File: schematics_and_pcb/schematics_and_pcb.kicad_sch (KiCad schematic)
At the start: 84 parts, among them J1 RND 205-00623, J2 RND 205-00627, SW1 RND 210-00210, U1 MIC5235YM5-TR, U2 AP2125N-3.3TRG1, U3 PWM3389DM-T3QU, U4 STM32F411RETx, Y1 YLFXTAL029370

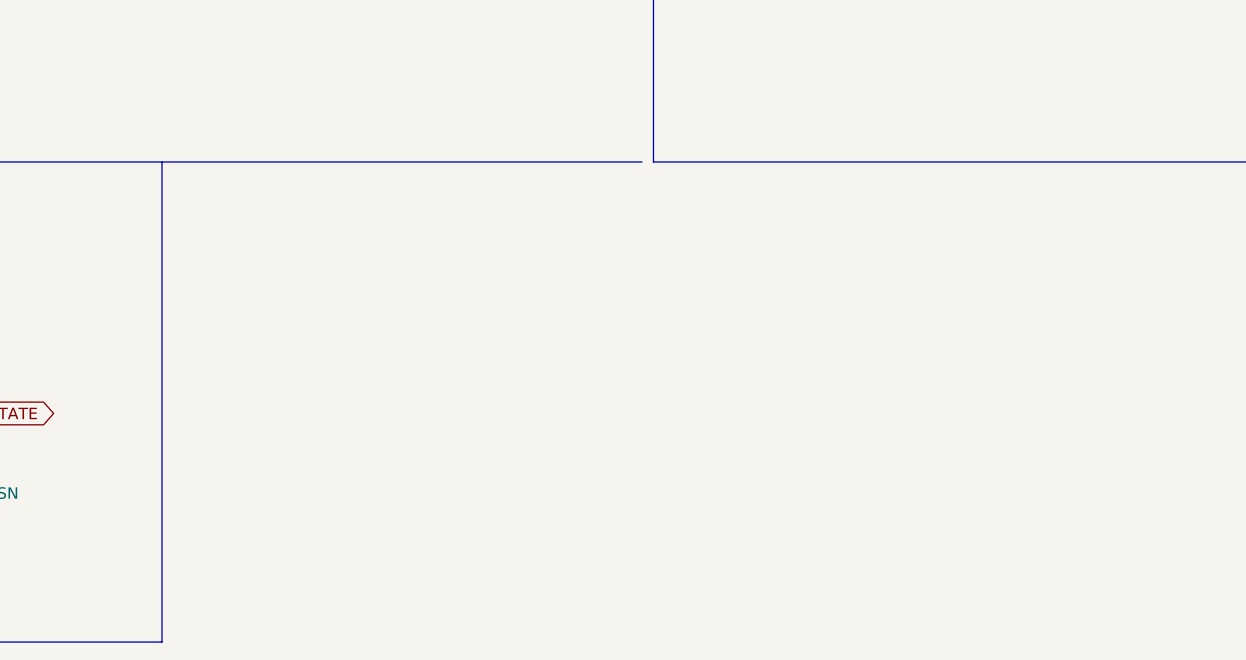
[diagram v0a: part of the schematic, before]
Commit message: added motor driver
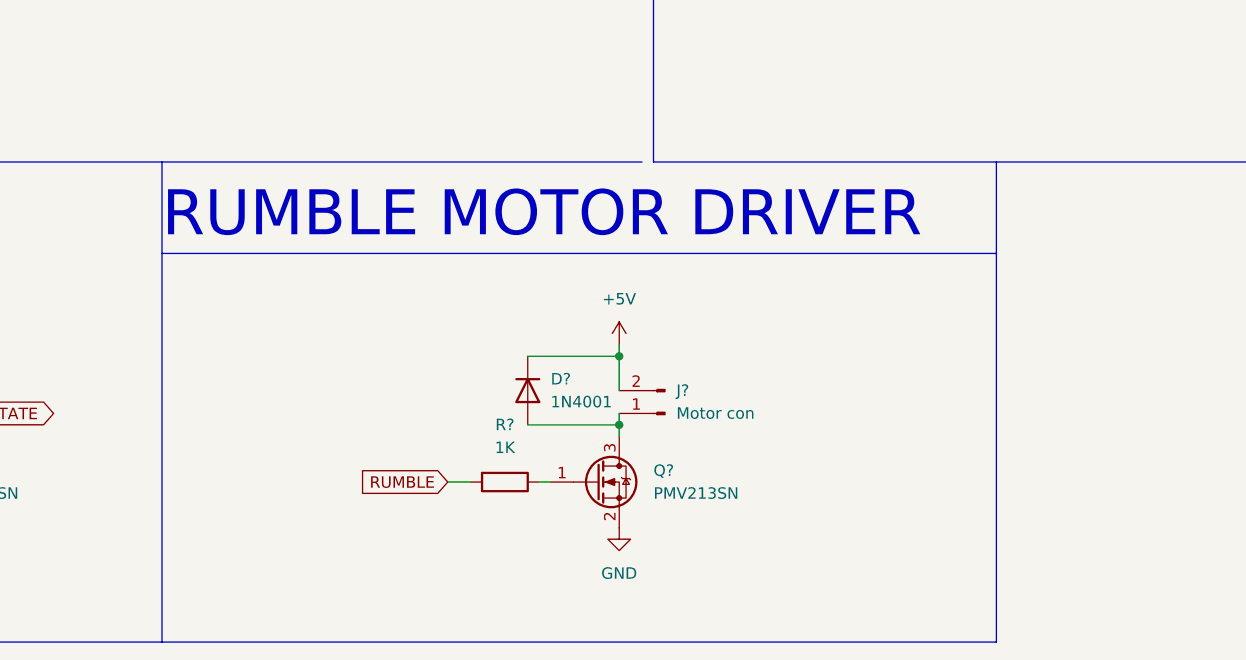
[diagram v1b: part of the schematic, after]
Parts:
- added D?: 1N4001, Diode_THT:D_DO-41_SOD81_P10.16mm_Horizontal, symbol Diode:1N4001
- added J?: Motor con, symbol Connector:Conn_01x02_Male
- added Q?: PMV213SN, symbol Device:Q_NMOS_GSD
- added R?: 1K, symbol Device:R
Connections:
- net +5V: now also D?.1 (K), J?.2 (Pin_2)
- net GND: now also Q?.2 (S)
- new net: D?.2 (A), J?.1 (Pin_1), Q?.3 (D)
- new net: Q?.1 (G), R?.1
- new net RUMBLE: R?.2
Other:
- note added: "RUMBLE MOTOR DRIVER"

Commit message: done with main board outline
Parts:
- removed C? (x2): 10u, Capacitor_SMD:C_0805_2012Metric_Pad1.18x1.45mm_HandSolder, symbol Device:C_Small
- removed Q? (x2): Q_NMOS_GSD, symbol Device:Q_NMOS_GSD
- removed Q? (x4): PMV213SN, symbol Device:Q_NMOS_GSD
- removed R? (x6): 10k, symbol Device:R_Small
- added D1, D3, D4: S1A, Diode_SMD:D_SMA_Handsoldering, symbol Diode:1N4001
- added D2: 1N4001, Diode_SMD:D_SMA_Handsoldering, symbol Diode:1N4001
- BACK_SIDE1: renamed from BACK_SIDE; footprint D2F-01F -> mouse:D2F-01F
- D5: renamed from D?; value 1N4001 -> S1A; footprint Diode_THT:D_DO-41_SOD81_P10.16mm_Horizontal -> Diode_SMD:D_SMA_Handsoldering
- FRONT_SIDE1: renamed from FRONT_SIDE; footprint D2F-01F -> mouse:D2F-01F
- J3: renamed from J?; footprint (none) -> Connector_PinSocket_2.54mm:PinSocket_1x02_P2.54mm_Vertical
- LED1, LED2, LED3, LED4, LED5, LED6, LED7, LED8: renamed from LED?; footprint (none) -> mouse:RND_135-00249
- LEFT_BUTTON1: renamed from LEFT_BUTTON; footprint D2F-01F -> mouse:D2F-01F
- Q1: renamed from Q?; footprint (none) -> Package_TO_SOT_SMD:SOT-23
- R11, R12, R13, R14, R15: renamed from R?; footprint (none) -> Resistor_SMD:R_0805_2012Metric_Pad1.20x1.40mm_HandSolder
- R4, R7: footprint (none) -> Resistor_SMD:R_0805_2012Metric_Pad1.20x1.40mm_HandSolder
- RIGHT_BUTTON1: renamed from RIGHT_BUTTON; footprint D2F-01F -> mouse:D2F-01F
- USB1: footprint Connector_USB:USB_Mini-B_Tensility_54-00023_Vertical -> Connector_PinSocket_2.54mm:PinSocket_1x06_P2.54mm_Vertical
- gave numbers to parts that had none: 5
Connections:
- net +5V: now also D1.1 (K), D2.1 (K), D3.1 (K), D4.1 (K)
- net BACK_STATE: now also BACK_SIDE1.2, C22.2, R12.2, U4.59 (PB7), D4.2 (A)
- net FRONT_STATE: now also C21.2, FRONT_SIDE1.2, R11.2, U4.58 (PB6), D3.2 (A)
- net LEFT_STATE: now also C19.2, LEFT_BUTTON1.2, R4.2, U4.56 (PB4), D1.2 (A)
- net PHASE_A: now also R14.1, U4.61 (PB8), enc1.A
- net PHASE_B: now also R15.1, U4.62 (PB9), enc1.B
- net RIGHT_STATE: now also C20.2, R7.2, RIGHT_BUTTON1.2, U4.57 (PB5), D2.2 (A)
- no-connect marks 40 -> 82
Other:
- moved on the sheet: C13, C14, C15, C16, C17, C18, C19, C20, C21, C22, FRONT_SIDE1, LEFT_BUTTON1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

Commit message: new layout
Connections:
- net RUMBLE: now also U4.2 (PC13)
- no-connect marks 82 -> 81
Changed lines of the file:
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@@
   (no_connect (at 22.86 41.91))
   (no_connect (at 346.71 78.74))
+  (no_connect (at 233.68 105.41))
   (no_connect (at 321.31 67.31))
   (no_connect (at 340.36 67.31))
@@
   (no_connect (at 233.68 95.25))
   (no_connect (at 346.71 62.23))
-  (no_connect (at 233.68 105.41))
   (no_connect (at 365.76 64.77))
   (no_connect (at 346.71 52.07))
@@
   (no_connect (at 233.68 74.93))
   (no_connect (at 233.68 133.35))
-  (no_connect (at 198.12 130.81))
   (no_connect (at 198.12 113.03))
   (no_connect (at 198.12 115.57))
@@
       (effects (font (size 1.27 1.27)) (justify right) hide)
     )
+  )
+  (global_label "RUMBLE" (shape output) (at 198.12 130.81 180) (fields_autoplaced)
+    (effects (font (size 1.27 1.27)) (justify right))
+    (property "Intersheet References" "${INTERSHEET_REFS}" (id 0) (at 188.2079 130.8894 0)
+      (effects (font (size 1.27 1.27)) (justify right) hide)
+    )

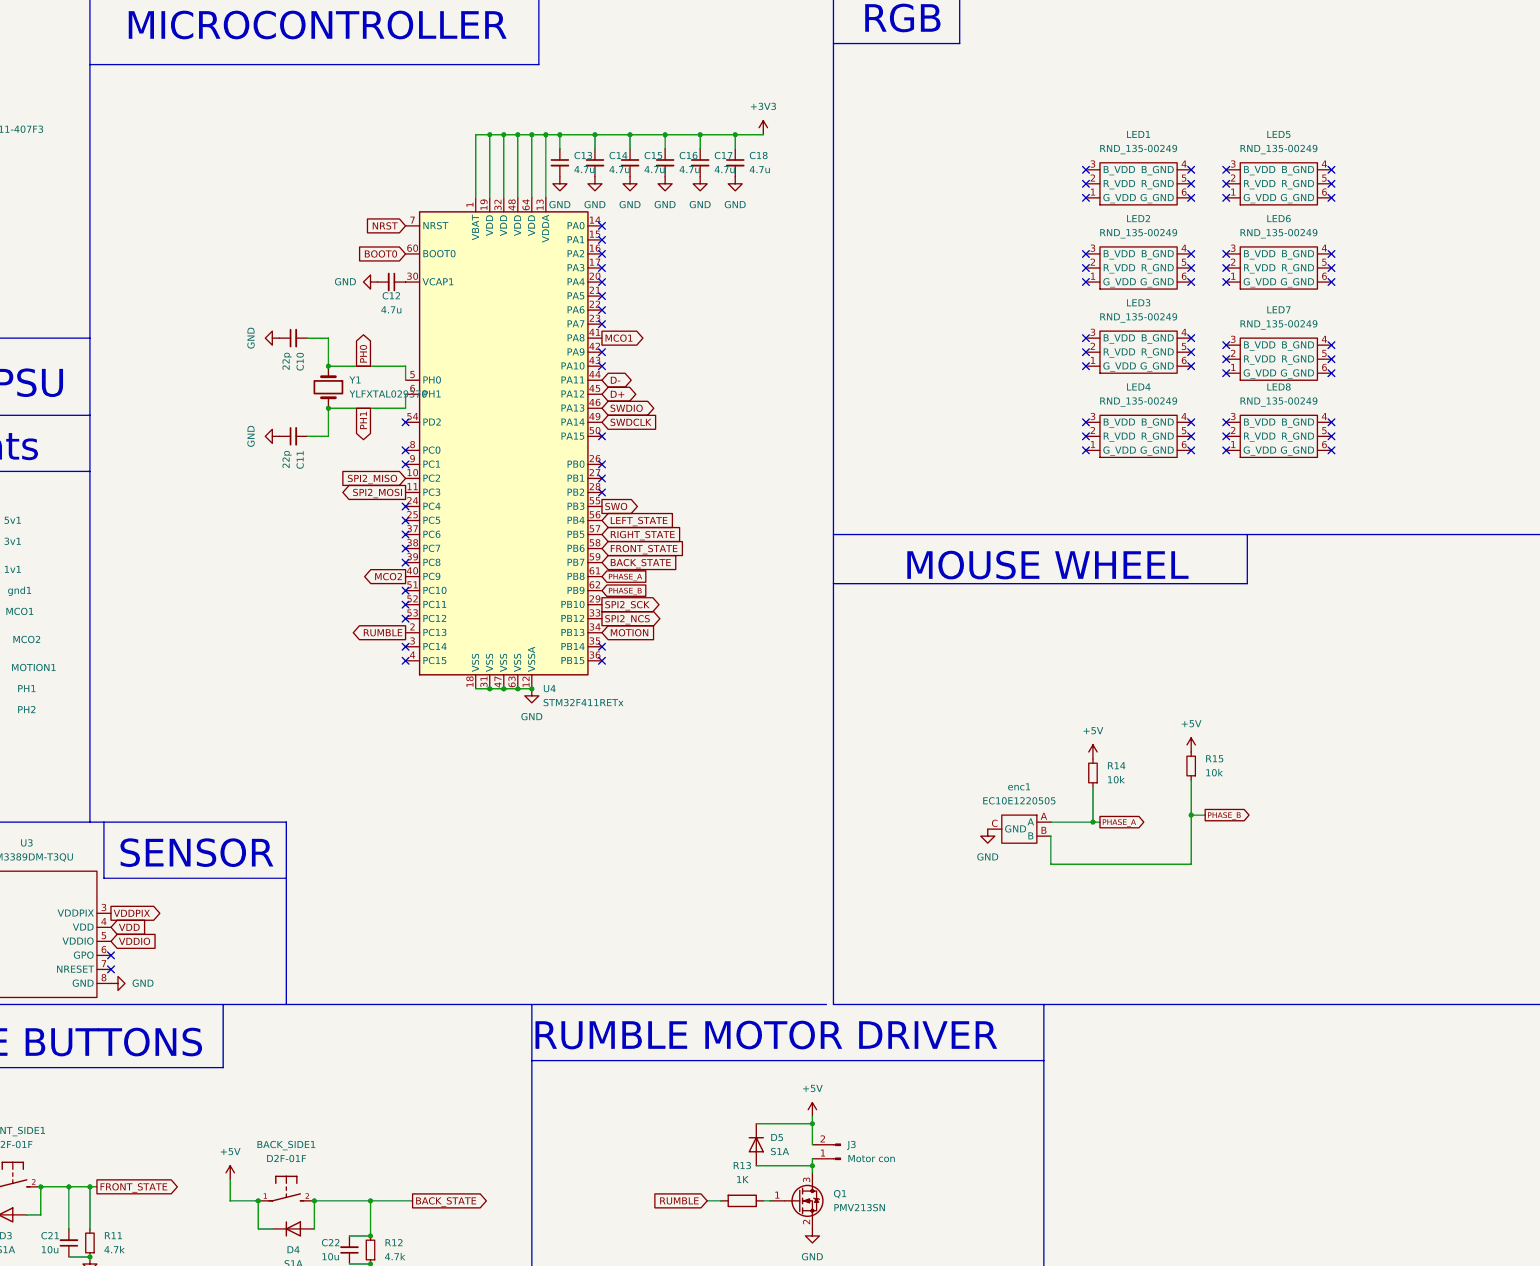
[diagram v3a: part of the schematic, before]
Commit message: added mounting holes
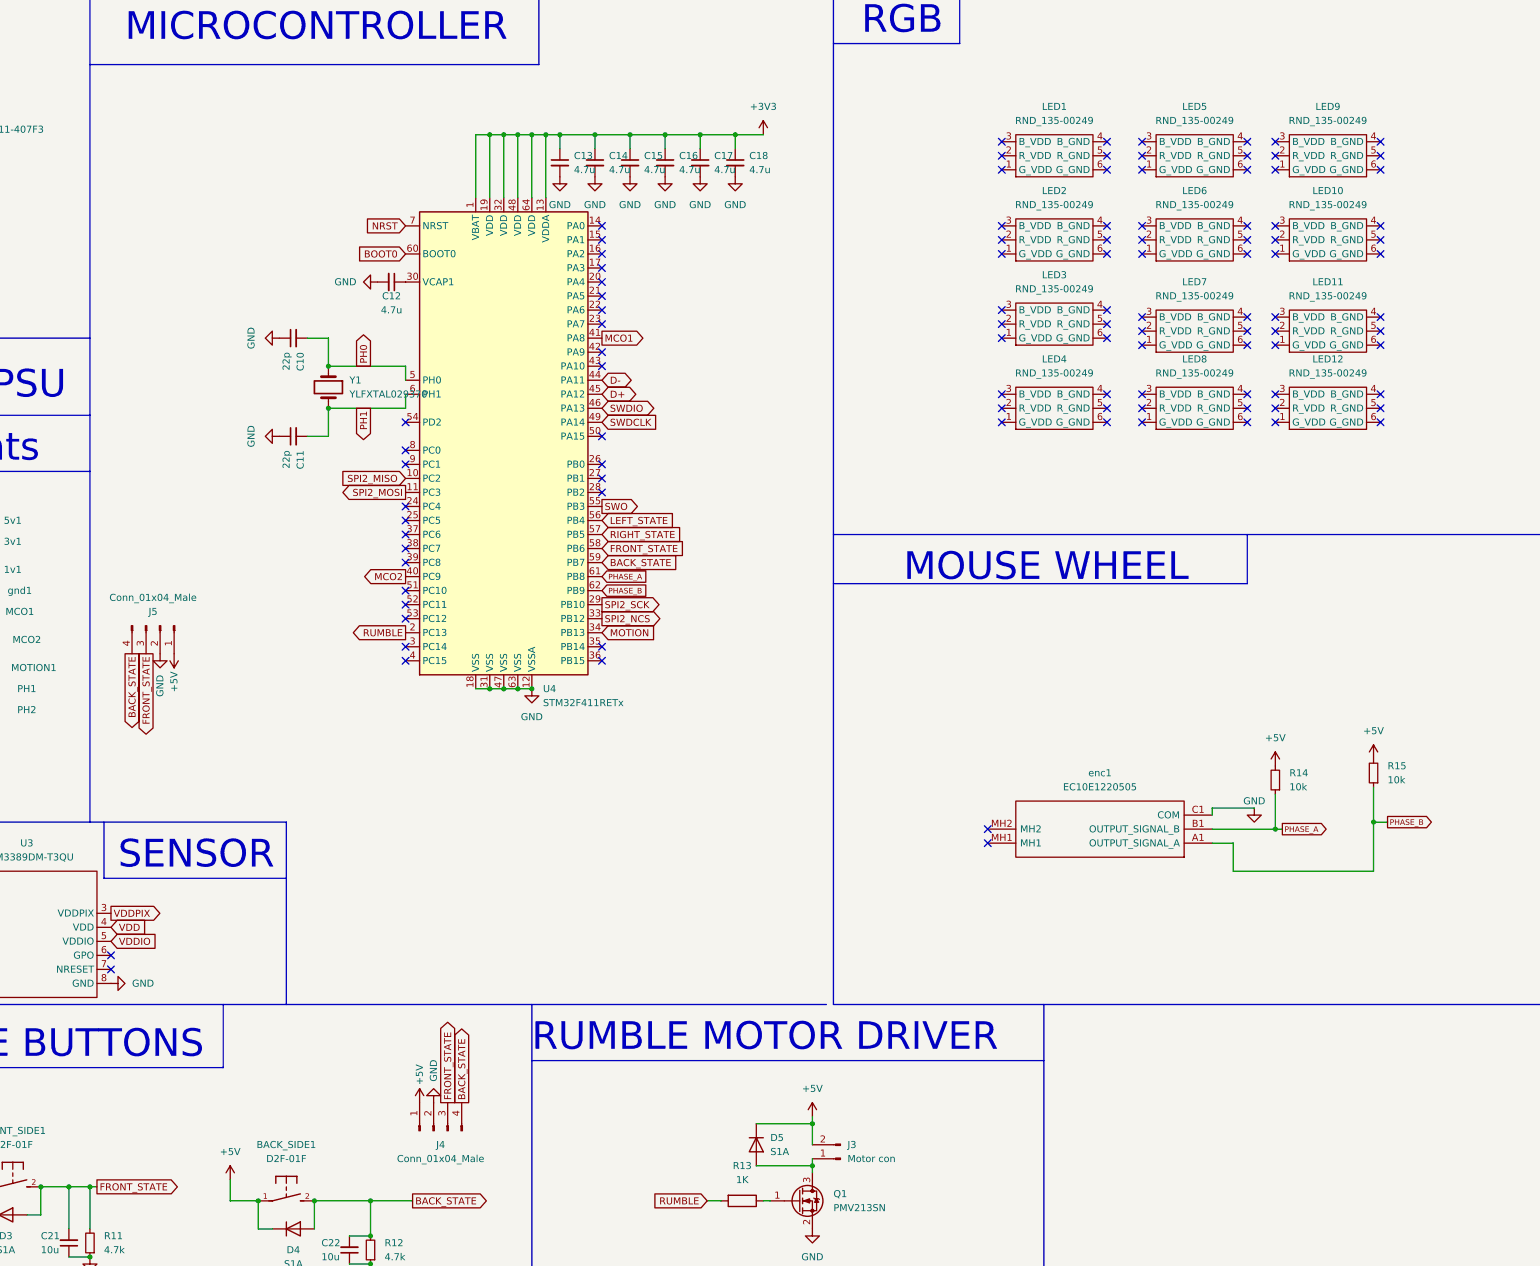
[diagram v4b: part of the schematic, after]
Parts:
- added J4, J5: Conn_01x04_Male, Connector_PinHeader_2.54mm:PinHeader_1x04_P2.54mm_Vertical, symbol Connector:Conn_01x04_Male
- added LED10, LED11, LED12, LED9: RND_135-00249, mouse:RND_135-00249, symbol mouse:RND_135-00249
- enc1: footprint (none) -> mouse:EC10E1220505; Height (none) -> 10.6; Manufacturer_Name (none) -> ALPS Electric; Manufacturer_Part_Number (none) -> EC10E1220505; Mouser Part Number (none) -> 688-EC10E1220505; Mouser Price/Stock (none) -> https://www.mouser.co.uk/ProductDetail/Alps-Alpine/EC10E122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
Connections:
- net +5V: now also J4.1 (Pin_1), J5.1 (Pin_1)
- net BACK_STATE: now also J4.4 (Pin_4), J5.4 (Pin_4)
- net FRONT_STATE: now also J4.3 (Pin_3), J5.3 (Pin_3)
- net GND: now also enc1.C1 (COM), J4.2 (Pin_2), J5.2 (Pin_2); no longer enc1.C (GND)
- net PHASE_A: now also enc1.B1 (OUTPUT_SIGNAL_B); no longer enc1.A
- net PHASE_B: now also enc1.A1 (OUTPUT_SIGNAL_A); no longer enc1.B
- no-connect marks 81 -> 107
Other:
- moved on the sheet: LED1, LED2, LED3, LED4, LED5, LED6, LED7, LED8, R14, R15
